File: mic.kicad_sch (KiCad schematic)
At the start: 6 parts, among them J5 J_000003

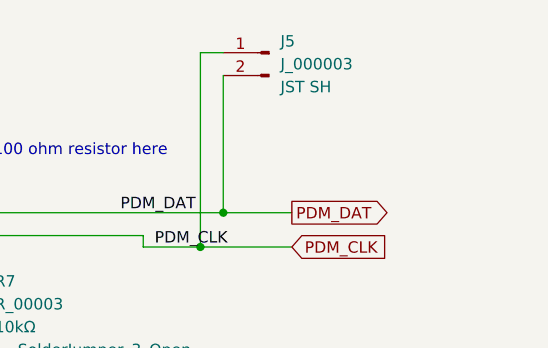
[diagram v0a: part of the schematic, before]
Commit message: Re routed power, placed Nora b106 module
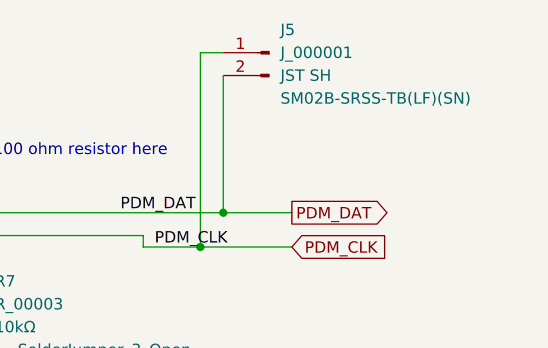
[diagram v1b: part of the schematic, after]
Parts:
- J5: value J_000003 -> J_000001; footprint mic_patch_parts:J_00003 -> mic_patch_parts:J_000001; symbol mic_patch_parts:J_00003 -> mic_patch_parts:J_000001; LCSC PNs C7430451 -> C160402; MPNs (none) -> SM02B-SRSS-TB(LF)(SN)
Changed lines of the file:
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@@
 	)
 	(symbol
-		(lib_id "mic_patch_parts:J_00003")
+		(lib_id "mic_patch_parts:J_000001")
 		(at 152.4 73.66 0)
 		(unit 1)
@@
 		(fields_autoplaced yes)
 		(property "Reference" "J5"
-			(at 157.48 67.3099 0)
+			(at 157.48 66.0399 0)
 			(effects
 				(font
@@
 			)
 		)
-		(property "Value" "J_000003"
-			(at 157.48 69.8499 0)
+		(property "Value" "J_000001"
+			(at 157.48 68.5799 0)
 			(effects
 				(font
@@
 			)
 		)
-		(property "Footprint" "mic_patch_parts:J_00003"
+		(property "Footprint" "mic_patch_parts:J_000001"
 			(at 159.004 81.788 0)
 			(effects
@@
 			)
 		)
-		(property "Description" "JST SH 2 Pin Straight Connector"
+		(property "Description" "JST SH 2 Right Angled Pin Connector"
 			(at 155.194 62.484 0)
 			(effects
@@
 		)
 		(property "Desc" "JST SH"
-			(at 157.48 72.3899 0)
+			(at 157.48 71.1199 0)
 			(effects
 				(font
@@
 			)
 		)
-		(property "LCSC PNs" "C7430451"
+		(property "LCSC PNs" "C160402"
 			(at 153.924 75.438 0)
 			(effects
@@
 			)
 		)
+		(property "MPNs" "SM02B-SRSS-TB(LF)(SN) "
+			(at 157.48 73.6599 0)
+			(effects
+				(font
+					(size 1.27 1.27)
+				)
+				(justify left)
+			)
+		)

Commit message: Re routed Mems microphone, added 100ohm termination resistor on PDM_DAT, changed pins
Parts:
- added R1: R_00005, Resistor_SMD:R_0402_1005Metric, symbol mic_patch_parts:R_00005
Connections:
- net PDM_DAT: now also R1.2; no longer MK1.1 (DATA)
- new net: MK1.1 (DATA), R1.1
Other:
- note added: "Place Near Mic"
- note removed: "Can add a 100 ohm resistor here"
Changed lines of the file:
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@@
 	(paper "A4")
+	(junction
+		(at 151.13 86.36)
+		(diameter 0)
+		(color 0 0 0 0)
+	)
 	(junction
 		(at 109.22 99.06)
@@
 	)
 	(junction
-		(at 151.13 86.36)
-		(diameter 0)
-		(color 0 0 0 0)
-	)
-	(junction
 		(at 80.01 81.28)
 		(diameter 0)
@@
 	(wire
 		(pts
+			(xy 135.89 86.36) (xy 151.13 86.36)
+		)
+		(stroke
+			(width 0)
+			(type default)
+		)
+	)
+	(wire
+		(pts
+			(xy 119.38 86.36) (xy 130.81 86.36)
+		)
+		(stroke
+			(width 0)
+			(type default)
+		)
+	)
+	(wire
+		(pts
 			(xy 66.04 99.06) (xy 80.01 99.06)
 		)
@@
 	(wire
 		(pts
-			(xy 119.38 86.36) (xy 151.13 86.36)
-		)
-		(stroke
-			(width 0)
-			(type default)
-		)
-	)
-	(wire
-		(pts
 			(xy 109.22 74.93) (xy 109.22 81.28)
 		)
@@
 		)
 	)
-	(text "Can add a 100 ohm resistor here\n"
+	(text "\nPlace Near Mic"
 		(exclude_from_sim no)
-		(at 130.556 79.502 0)
+		(at 130.81 75.692 0)
 		(effects
 			(font
@@
 					(unit 1)
 				)
+			)
+		)
+	)
+	(symbol
+		(lib_id "mic_patch_parts:R_00005")
+		(at 133.35 86.36 90)
+		(unit 1)
+		(exclude_from_sim no)
+		(in_bom yes)
+		(on_board yes)
+		(dnp no)
+		(fields_autoplaced yes)
+		(property "Reference" "R1"
+			(at 133.35 78.74 90)
+			(effects
+				(font
+					(size 1.27 1.27)
+				)
+			)
+		)
+		(property "Value" "R_00005"
+			(at 133.35 81.28 90)
+			(effects
+				(font
+					(size 1.27 1.27)
+				)
+			)
+		)
+		(property "Footprint" "Resistor_SMD:R_0402_1005Metric"
+			(at 133.35 86.36 0)
+			(effects
+				(font
+					(size 1.27 1.27)
+				)
+				(hide yes)
+			)
+		)
+		(property "Datasheet" "~"
+			(at 133.35 86.36 0)
+			(effects
+				(font
+					(size 1.27 1.27)
+				)
+				(hide yes)
+			)
+		)
+		(property "Description" "100Ω resistor"
+			(at 133.35 86.36 0)
+			(effects
+				(font
+					(size 1.27 1.27)
+				)
+				(hide yes)
+			)
+		)
+		(property "Desc" "100Ω "
+			(at 133.35 83.82 90)
+			(effects
+				(font
+					(size 1.27 1.27)
+				)
+			)
+		)
+		(property "MPNs" "0402WGF1000TCE"
+			(at 133.35 86.36 0)
+			(effects
+				(font
+					(size 1.27 1.27)
+				)
+				(hide yes)
+			)
+		)
+		(property "LCSC PNs" "C25076"
+			(at 133.35 86.36 0)
+			(effects
+				(font
+					(size 1.27 1.27)
+				)
+				(hide yes)
+			)
+		)
+		(pin "1"
+		)
+		(pin "2"
+		)
+		(instances
+			(project "mic_patch_v1"
+				(path "/5448a297-4261-40a5-8009-47199bfe22cb/134a282e-9ca3-4100-8ce3-f798951ef007"
+					(reference "R1")
+					(unit 1)
+				)
